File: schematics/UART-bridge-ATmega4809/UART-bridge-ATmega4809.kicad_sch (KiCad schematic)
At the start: 17 parts, among them J1 UPDI connector, J2 To Pad/Memcard connectors, J3 External 7.5V power suply, SW1 Reset, U1 ATmega4809-P, U2 7.5 to 3.5 DC-DC, U3 USB-UART adapter

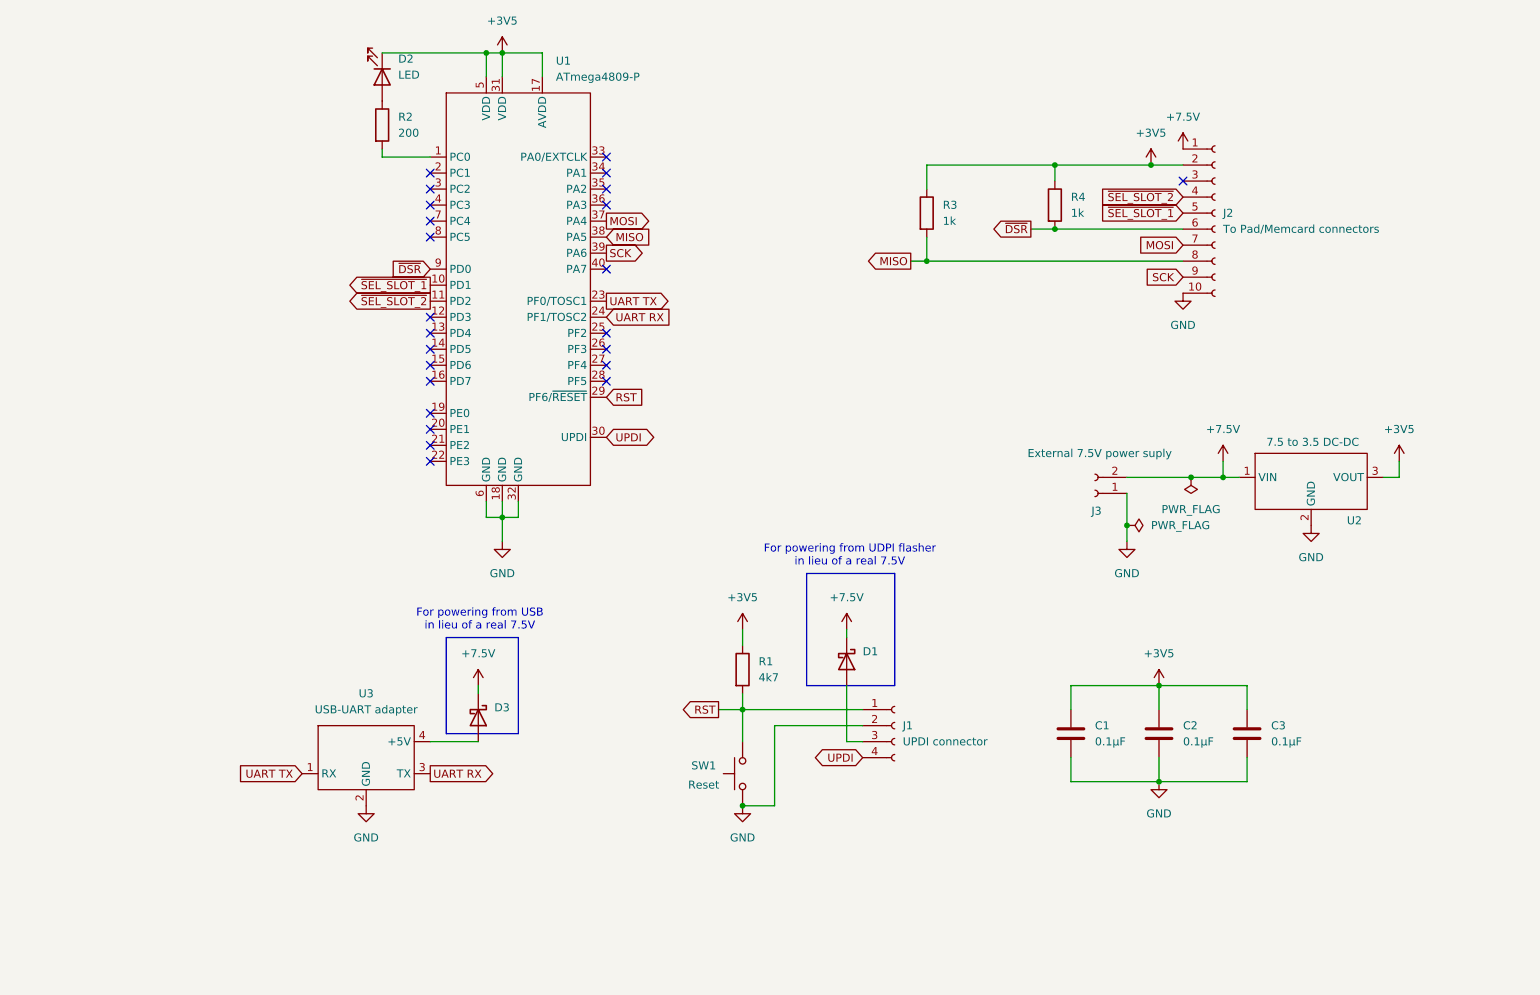
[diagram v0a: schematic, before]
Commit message: Tweak schematics, add IRQ pin for future-proofing
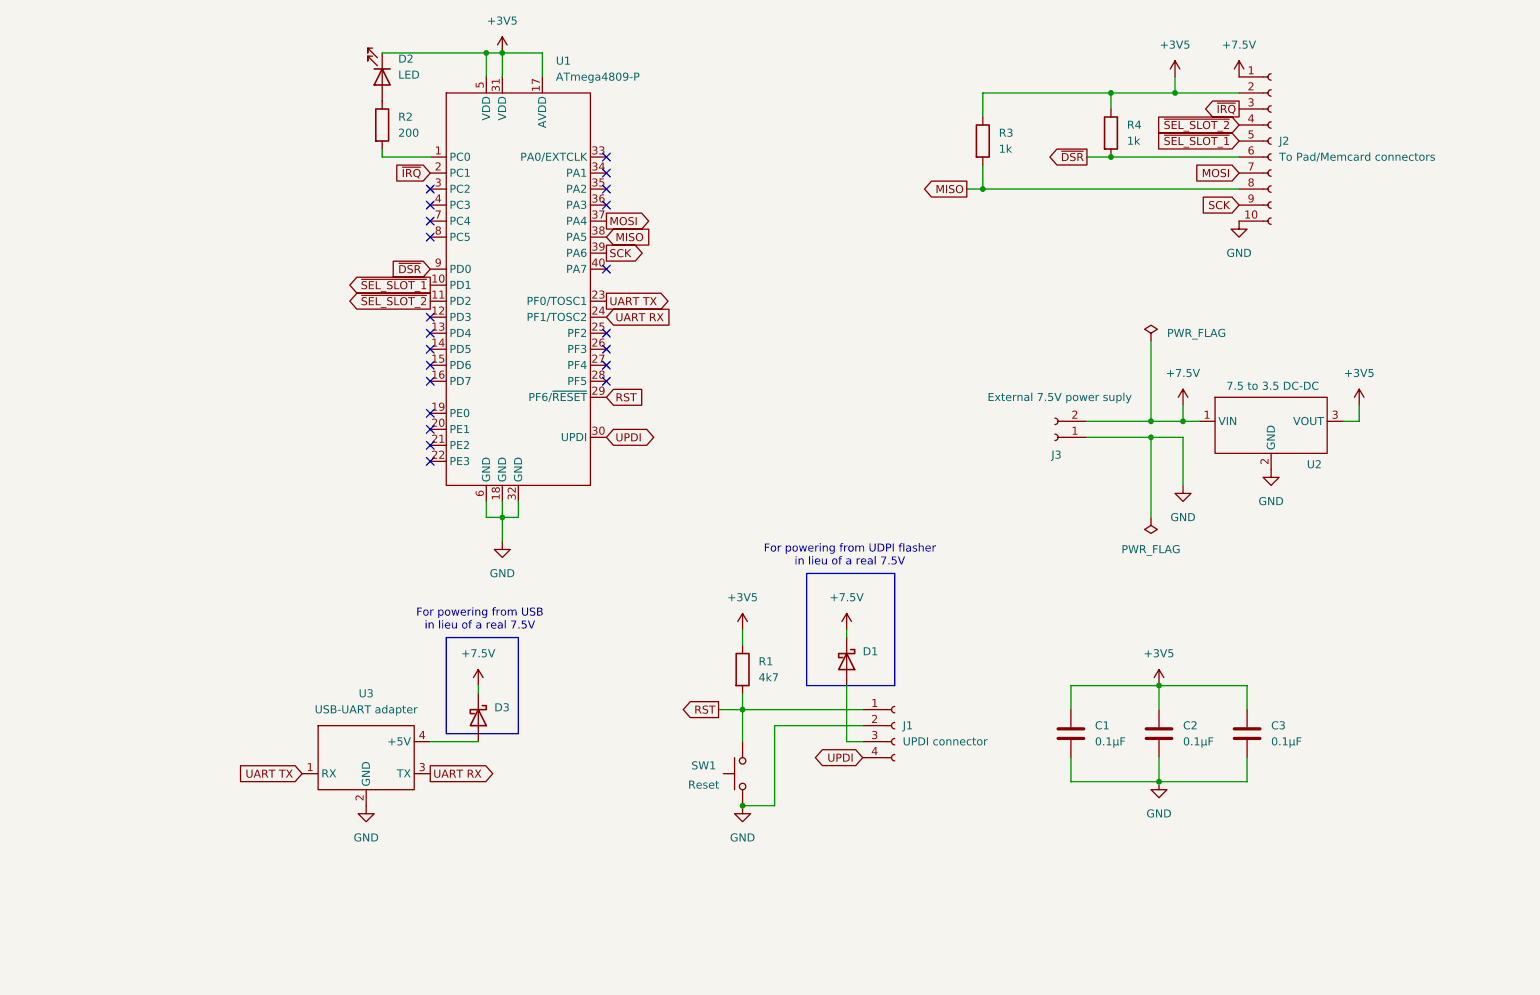
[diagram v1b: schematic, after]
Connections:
- net ~{IRQ}: now reaches U1.2 (PC1)
- net ~{IRQ}: now also J2.3 (Pin_3)
- no-connect marks 24 -> 22
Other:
- moved on the sheet: J2, J3, R3, R4, U2

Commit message: Design PCB prototype
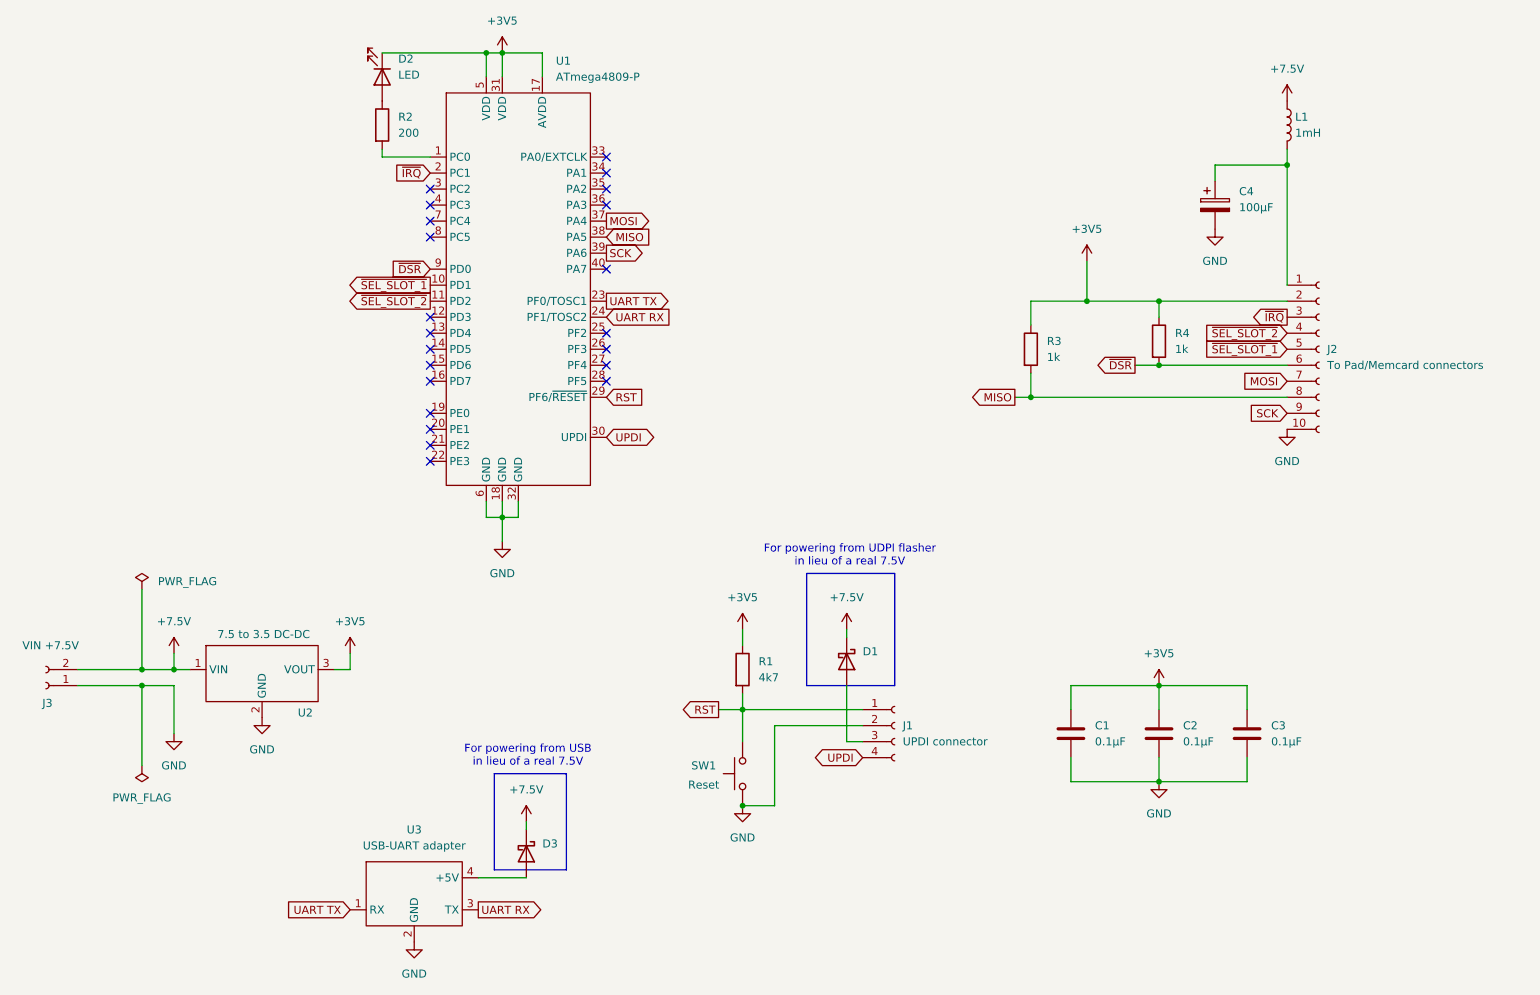
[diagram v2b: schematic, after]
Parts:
- added C4: 100µF, Capacitor_THT:C_Radial_D5.0mm_H11.0mm_P2.00mm, symbol Device:C_Polarized
- added L1: 1mH, Inductor_THT:L_Radial_D7.0mm_P3.00mm, symbol Device:L
- C1, C2, C3: footprint (none) -> Capacitor_THT:C_Disc_D5.0mm_W2.5mm_P5.00mm
- D1, D3: footprint (none) -> Diode_THT:D_A-405_P7.62mm_Horizontal
- D2: footprint (none) -> LED_THT:LED_D5.0mm_Clear
- J1: footprint (none) -> Connector_PinSocket_2.54mm:PinSocket_1x04_P2.54mm_Vertical
- J2: footprint (none) -> Connector_PinSocket_2.54mm:PinSocket_1x10_P2.54mm_Vertical
- J3: value External 7.5V power suply -> VIN +7.5V; footprint (none) -> Connector_PinSocket_2.54mm:PinSocket_1x02_P2.54mm_Vertical
- R1, R2, R3, R4: footprint (none) -> Resistor_THT:R_Axial_DIN0207_L6.3mm_D2.5mm_P7.62mm_Horizontal
- SW1: footprint (none) -> Button_Switch_THT:SW_PUSH_6mm
- U1: footprint (none) -> Package_DIP:DIP-40_W15.24mm_Socket
- U2: footprint (none) -> Connector_PinSocket_2.54mm:PinSocket_1x03_P2.54mm_Vertical
- U3: footprint (none) -> Connector_PinSocket_2.54mm:PinSocket_1x06_P2.54mm_Vertical
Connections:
- net +7.5V: now also L1.1; no longer J2.1 (Pin_1)
- net GND: now also C4.2
- new net: C4.1, J2.1 (Pin_1), L1.2
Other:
- moved on the sheet: D3, J2, J3, R3, R4, U2, U3
